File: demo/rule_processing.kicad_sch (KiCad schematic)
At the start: 0 parts

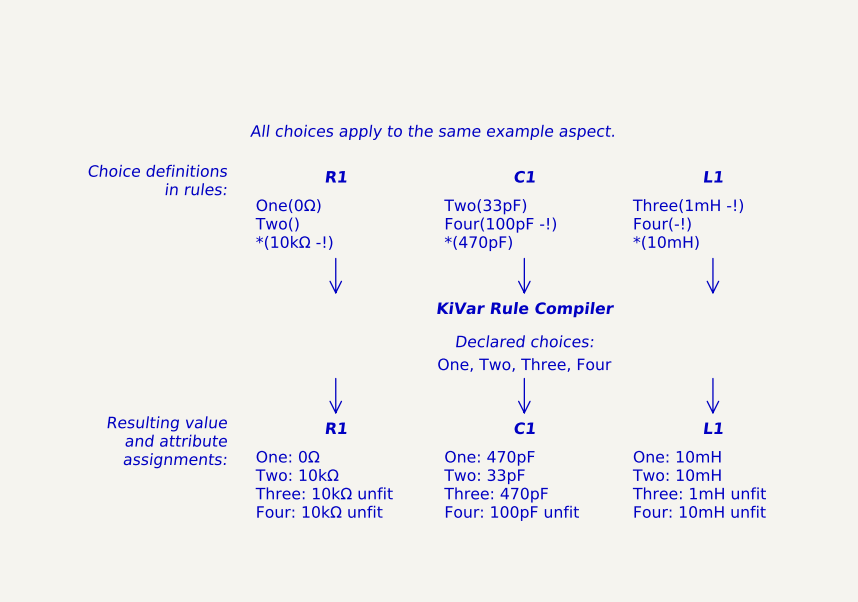
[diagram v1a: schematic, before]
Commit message: Make use of new 0.2.0 features in demo project, use different expression types
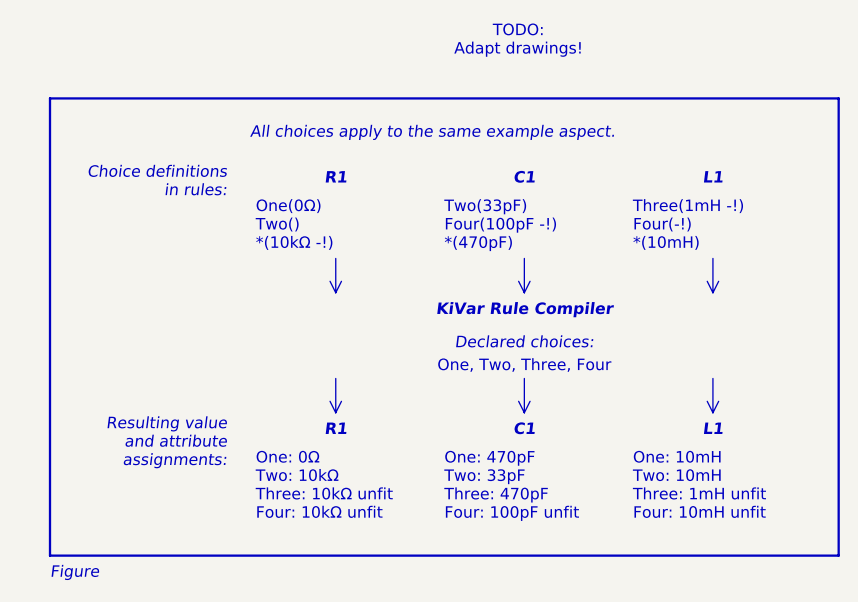
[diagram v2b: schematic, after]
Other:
- note added: "Figure"
- note added: "TODO: Adapt drawings!"
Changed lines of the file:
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@@
+		)
+	)
+	(rectangle
+		(start 49.53 33.02)
+		(end 137.16 83.82)
+		(stroke
+			(width 0.254)
+			(type default)
+			(color 72 72 72 1)
+		)
+		(fill
+			(type none)
 		)
 	)
@@
 			)
 			(justify left top)
+		)
+	)
+	(text "TODO:\nAdapt drawings!"
+		(exclude_from_sim no)
+		(at 101.6 26.67 0)
+		(effects
+			(font
+				(size 1.27 1.27)
+			)
+		)
+	)
+	(text "Figure"
+		(exclude_from_sim no)
+		(at 49.53 85.09 0)
+		(effects
+			(font
+				(size 1.27 1.27)
+				(italic yes)
+				(color 72 72 72 1)
+			)
+			(justify left top)

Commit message: Remove outdated rule structure figure, update compiler figure
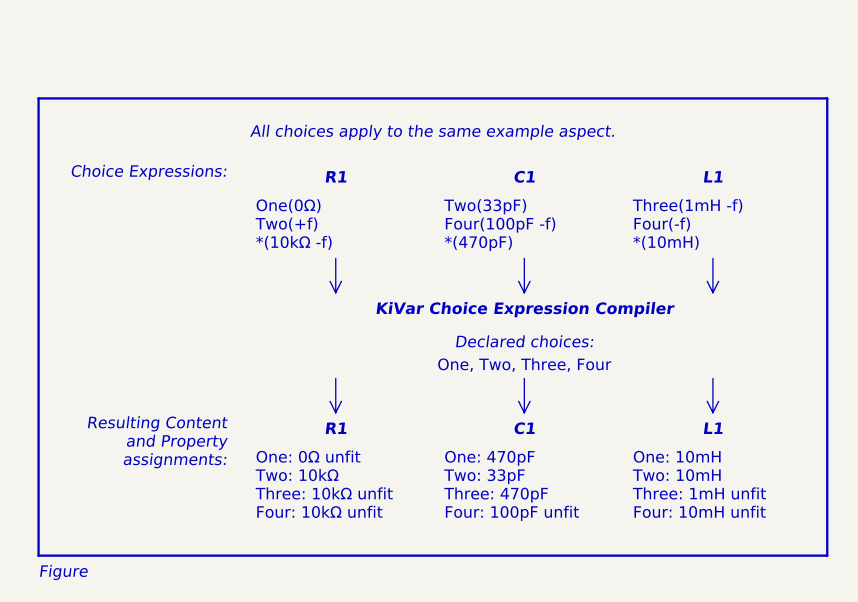
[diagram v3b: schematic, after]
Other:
- note added: "Choice Expressions:"
- note added: "One(0Ω) Two(+f) *(10kΩ -f)"
- note added: "One: 0Ω unfit Two: 10kΩ Three: 10kΩ unfit Four: 10kΩ unfit"
- note added: "Resulting Content and Property assignments:"
- note added: "Three(1mH -f) Four(-f) *(10mH)"
- note added: "Two(33pF) Four(100pF -f) *(470pF)"
- note removed: "Choice definitions in rules:"
- note removed: "One(0Ω) Two() *(10kΩ -!)"
- note removed: "One: 0Ω Two: 10kΩ Three: 10kΩ unfit Four: 10kΩ unfit"
- note removed: "Resulting value and attribute assignments:"
- note removed: "TODO: Adapt drawings!"
- note removed: "Three(1mH -!) Four(-!) *(10mH)"
- note removed: "Two(33pF) Four(100pF -!) *(470pF)"
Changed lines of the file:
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@@
 	)
 	(rectangle
-		(start 49.53 33.02)
-		(end 137.16 83.82)
+		(start 48.26 33.02)
+		(end 135.89 83.82)
 		(stroke
 			(width 0.254)
@@
 		)
 	)
-	(text_box "KiVar Rule Compiler"
+	(text_box "KiVar Choice Expression Compiler"
 		(exclude_from_sim no)
 		(at 71.755 54.61 0)
@@
 		)
 	)
-	(text "Two(33pF)\nFour(100pF -!)\n*(470pF)"
+	(text "Two(33pF)\nFour(100pF -f)\n*(470pF)"
 		(exclude_from_sim no)
 		(at 93.345 44.45 0)
@@
 		)
 	)
-	(text "Three(1mH -!)\nFour(-!)\n*(10mH)"
+	(text "Three(1mH -f)\nFour(-f)\n*(10mH)"
 		(exclude_from_sim no)
 		(at 114.3 44.45 0)
@@
 		)
 	)
-	(text "TODO:\nAdapt drawings!"
-		(exclude_from_sim no)
-		(at 101.6 26.67 0)
-		(effects
-			(font
-				(size 1.27 1.27)
-			)
-		)
-	)
 	(text "Figure"
 		(exclude_from_sim no)
-		(at 49.53 85.09 0)
+		(at 48.26 85.09 0)
 		(effects
 			(font
@@
 		)
 	)
-	(text "One: 0Ω\nTwo: 10kΩ\nThree: 10kΩ unfit\nFour: 10kΩ unfit"
+	(text "One: 0Ω unfit\nTwo: 10kΩ\nThree: 10kΩ unfit\nFour: 10kΩ unfit"
 		(exclude_from_sim no)
 		(at 72.39 72.39 0)
@@
 		)
 	)
-	(text "Resulting value\nand attribute\nassignments:"
+	(text "Resulting Content\nand Property\nassignments:"
 		(exclude_from_sim no)
 		(at 69.215 68.58 0)
@@
 		)
 	)
-	(text "Choice definitions\nin rules:"
+	(text "Choice Expressions:"
 		(exclude_from_sim no)
 		(at 69.215 40.64 0)
@@
 		)
 	)
-	(text "One(0Ω)\nTwo()\n*(10kΩ -!)"
+	(text "One(0Ω)\nTwo(+f)\n*(10kΩ -f)"
 		(exclude_from_sim no)
 		(at 72.39 44.45 0)
